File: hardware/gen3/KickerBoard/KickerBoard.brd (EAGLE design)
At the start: 130 x 100 mm, 104 parts, among them Q6 MOSFET-PCHANNEL, U1 NC7WZ08K8X, U2 ATMEGA165PV-8AU

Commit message: regulator
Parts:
- removed 5REG: (no value), SparkFun-PowerIC:SOT23-5
- removed C7: 470pF, SparkFun-Capacitors:0805
- added U$6: 3.3REG1A, gen3:3.3REG1A
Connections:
- removed net N$16: 5REG.4, C7.1
- net 12V: now also U$6.FIN, U$6.IN; no longer 5REG.1, 5REG.3
- net 5V: now also U$6.OUT; no longer 5REG.5
- net GND: now also U$6.NC; no longer 5REG.2, C7.2
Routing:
- net 12V: track 403.9 -> 394.5 mm
- net GND: track 496.7 -> 493.5 mm
- net N$16: track 3.19 -> 0.00 mm
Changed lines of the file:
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@@
 <attribute name="PROD_ID" value="VREG-00822" x="-55.12" y="144.31" size="1.778" layer="27" rot="R180" display="off"/>
-</element>
-<element name="5REG" library="SparkFun-PowerIC" package="SOT23-5" value="" x="16" y="21.5">
-<attribute name="PROD_ID" value="VREG-00823" x="90.93" y="-109.31" size="1.778" layer="27" display="off"/>
 </element>
 <element name="BATT" library="con-wago-500" package="W237-102" value="" x="38" y="7">
@@
 <element name="PWM_FILT" library="gen3" package="TESTING_PT" value="TEST_PT" x="58.2" y="66" rot="R180"/>
 <element name="DIS" library="gen3" package="TESTING_PT" value="TEST_PT" x="112" y="15"/>
-<element name="C7" library="SparkFun-Capacitors" package="0805" value="470pF" x="20" y="20.5"/>
 <element name="C8" library="SparkFun-Capacitors" package="0805" value="470pF" x="20" y="14.5"/>
 <element name="C10" library="gen3" package="PANASONIC_D" value="100uF" x="26" y="12.5" rot="R270">
@@
 </element>
 <element name="R9" library="SparkFun-Passives" package="0805" value="10k" x="21.3" y="71.2" rot="R270"/>
+<element name="U$6" library="gen3" package="3.3REG1A" value="3.3REG1A" x="-104" y="6"/>
 </elements>
 <signals>
@@
 <wire x1="70.262" y1="66.5776" x2="70.262" y2="66.238" width="0.3048" layer="1"/>
 <wire x1="64.05" y1="67.95" x2="63.2499" y2="67.95" width="0.4064" layer="1"/>
-<contactref element="C7" pad="2"/>
 <contactref element="C8" pad="2"/>
 <contactref element="C10" pad="-"/>
@@
 <contactref element="C21" pad="2"/>
 <contactref element="3.3REG" pad="2"/>
-<contactref element="5REG" pad="2"/>
 <wire x1="39.76" y1="14.18" x2="39.0230875" y2="14.248475" width="6.4516" layer="1"/>
 <wire x1="39.0230875" y1="14.248475" x2="39.3962" y2="17.0472125" width="6.4516" layer="1"/>
@@
 <wire x1="24" y1="17.5" x2="23.25" y2="18.25" width="1.6764" layer="1"/>
 <wire x1="23.25" y1="18.25" x2="21" y2="20.5" width="1.6764" layer="1"/>
-<wire x1="21" y1="20.5" x2="20.9" y2="20.5" width="1.6764" layer="1"/>
 <wire x1="24" y1="17.5" x2="21" y2="14.5" width="1.6764" layer="1"/>
 <wire x1="21" y1="14.5" x2="20.9" y2="14.5" width="1.6764" layer="1"/>
-<wire x1="20.9" y1="20.5" x2="21" y2="22.6" width="1.6764" layer="1"/>
 <wire x1="20.9" y1="14.5" x2="20.4" y2="11.6" width="1.6764" layer="1"/>
-<wire x1="16" y1="20.1999" x2="16" y2="19.2" width="0.4064" layer="1"/>
 <wire x1="16" y1="19.2" x2="16.8" y2="18.4" width="0.4064" layer="1"/>
 <wire x1="16.8" y1="17.6" x2="16.8" y2="16.9" width="0.4064" layer="1"/>
@@
 <vertex x="6" y="99"/>
 </polygon>
+<contactref element="U$6" pad="NC"/>
+<wire x1="3.3" y1="7.7" x2="-104" y2="2.69" width="0" layer="19" extent="1-1"/>
+<wire x1="21" y1="22.6" x2="21" y2="20.5" width="0" layer="19" extent="1-1"/>
 </signal>
 <signal name="3.3V">
@@
 <contactref element="DRIB" pad="1"/>
 <contactref element="3.3REG" pad="3"/>
-<contactref element="5REG" pad="1"/>
-<contactref element="5REG" pad="3"/>
 <contactref element="3.3REG" pad="1"/>
 <contactref element="U$3" pad="P$5"/>
@@
 <wire x1="82.5" y1="67" x2="82.5" y2="68" width="1.778" layer="1"/>
 <wire x1="63.63" y1="36.63" x2="59.88" y2="36.63" width="1.778" layer="1"/>
-<wire x1="15.05" y1="20.1999" x2="15.05" y2="14.8001" width="0.6096" layer="1"/>
-<wire x1="15.05" y1="20.1999" x2="15" y2="20.1499" width="0.6096" layer="1"/>
 <wire x1="15" y1="20.1499" x2="15" y2="17.5" width="0.6096" layer="1"/>
 <via x="15" y="17.5" extent="1-16" drill="0.6" shape="square"/>
@@
 <wire x1="17.301" y1="54.699" x2="12.5" y2="54.699" width="3.81" layer="1"/>
 <wire x1="15" y1="17.5" x2="14.95" y2="17.5" width="1.6764" layer="1"/>
-<wire x1="16.95" y1="20.1999" x2="16.95" y2="21.05" width="0.4064" layer="1"/>
-<wire x1="16.95" y1="21.05" x2="16.5" y2="21.5" width="0.4064" layer="1"/>
-<wire x1="16.5" y1="21.5" x2="15.5" y2="21.5" width="0.4064" layer="1"/>
-<wire x1="15.5" y1="21.5" x2="15.1" y2="21.1" width="0.4064" layer="1"/>
-<wire x1="15.1" y1="21.1" x2="15.1" y2="20.2499" width="0.4064" layer="1"/>
-<wire x1="15.1" y1="20.2499" x2="15.05" y2="20.1999" width="0.4064" layer="1"/>
 <wire x1="15.05" y1="14.8001" x2="15.05" y2="13.85" width="0.4064" layer="1"/>
 <wire x1="15.05" y1="13.85" x2="15.4" y2="13.8" width="0.4064" layer="1"/>
@@
 <vertex x="5.5" y="99"/>
 </polygon>
+<contactref element="U$6" pad="FIN"/>
+<contactref element="U$6" pad="IN"/>
+<wire x1="-104" y1="8.5" x2="-106.28" y2="1.2" width="0" layer="19" extent="1-1"/>
+<wire x1="15.05" y1="13.85" x2="-104" y2="8.5" width="0" layer="19" extent="1-1"/>
+<wire x1="16.95" y1="17.5" x2="16.95" y2="14.8001" width="0" layer="19" extent="1-16"/>
 </signal>
 <signal name="12VGND">
@@
 </signal>
 <signal name="5V">
-<contactref element="5REG" pad="5"/>
 <contactref element="LOGIC_HEADER" pad="5"/>
 <contactref element="LOGIC_HEADER" pad="6"/>
@@
 <wire x1="25.7" y1="25.5" x2="21" y2="25.5" width="1.6764" layer="1"/>
 <wire x1="21" y1="25.5" x2="21" y2="24.4" width="0.6096" layer="1"/>
-<wire x1="15.05" y1="22.8001" x2="15" y2="22.8501" width="0.6096" layer="1"/>
 <wire x1="15" y1="22.8501" x2="15" y2="25.5" width="0.6096" layer="1"/>
 <wire x1="15" y1="25.5" x2="21" y2="25.5" width="1.6764" layer="1"/>
@@
 <wire x1="66.95" y1="73.7" x2="66.960646875" y2="72.989353125" width="1.27" layer="1"/>
 <wire x1="66.960646875" y1="72.989353125" x2="66.960646875" y2="69.385609375" width="1.27" layer="1"/>
+<contactref element="U$6" pad="OUT"/>
+<wire x1="8" y1="14.16" x2="-101.72" y2="1.2" width="0" layer="19" extent="1-1"/>
 </signal>
 <signal name="N$19">
@@
 <wire x1="22.7" y1="82.5" x2="22.4" y2="82.6" width="0.254" layer="1"/>
 </signal>
-<signal name="N$16">
-<contactref element="5REG" pad="4"/>
-<contactref element="C7" pad="1"/>
-<wire x1="16.95" y1="22.8001" x2="16.95" y2="22.65" width="0.4064" layer="1"/>
-<wire x1="16.95" y1="22.65" x2="19.1" y2="20.5" width="0.4064" layer="1"/>
-</signal>
 <signal name="N$18">

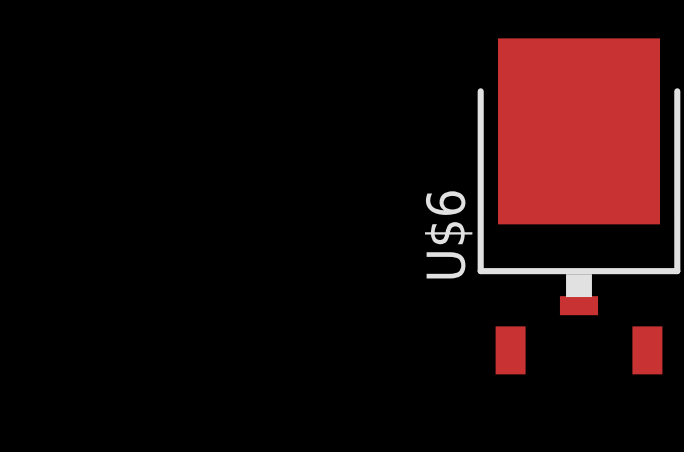
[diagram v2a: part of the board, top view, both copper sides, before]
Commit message: added decoupling to comms and kicker
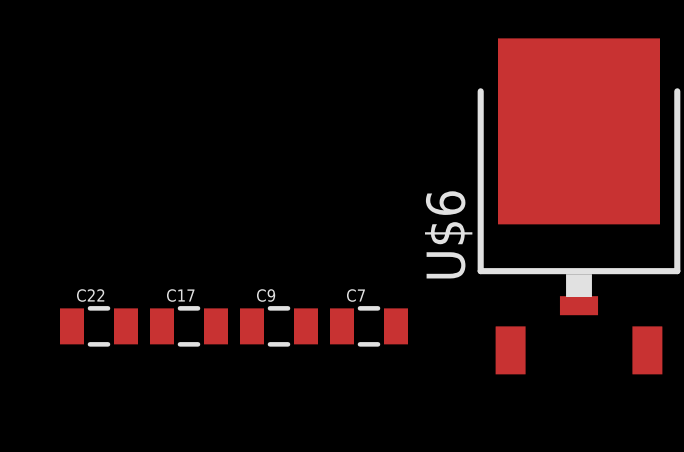
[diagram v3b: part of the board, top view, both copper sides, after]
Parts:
- added C17: 1uF, SparkFun-Capacitors:0805
- added C22, C7, C9: .01uF, SparkFun-Capacitors:0805
- C13, C14: value .1uF -> 1uF
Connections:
- net 3.3V: now also C17.1, C22.1, C7.1
- net 5V: now also C9.1
- net GND: now also C17.2, C22.2, C7.2, C9.2
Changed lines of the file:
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@@
 <element name="LED6" library="SparkFun-LED" package="LED-1206" value="" x="5" y="34" rot="R180"/>
 <element name="LED7" library="SparkFun-LED" package="LED-1206" value="" x="5" y="30" rot="R180"/>
-<element name="C13" library="SparkFun-Capacitors" package="0805" value=".1uF" x="20.4" y="10.7" rot="R90"/>
-<element name="C14" library="SparkFun-Capacitors" package="0805" value=".1uF" x="21" y="23.5" rot="R270"/>
+<element name="C13" library="SparkFun-Capacitors" package="0805" value="1uF" x="20.4" y="10.7" rot="R90"/>
+<element name="C14" library="SparkFun-Capacitors" package="0805" value="1uF" x="21" y="23.5" rot="R270"/>
 <element name="C15" library="SparkFun-Capacitors" package="0805" value=".1uF" x="54.65" y="65.75" rot="R270"/>
 <element name="C16" library="SparkFun-Capacitors" package="0805" value=".1uF" x="83" y="71"/>
@@
 <element name="R9" library="SparkFun-Passives" package="0805" value="10k" x="21.3" y="71.2" rot="R270"/>
 <element name="U$6" library="gen3" package="3.3REG1A" value="3.3REG1A" x="-104" y="6"/>
+<element name="C7" library="SparkFun-Capacitors" package="0805" value=".01uF" x="-111" y="2"/>
+<element name="C9" library="SparkFun-Capacitors" package="0805" value=".01uF" x="-114" y="2"/>
+<element name="C17" library="SparkFun-Capacitors" package="0805" value="1uF" x="-117" y="2"/>
+<element name="C22" library="SparkFun-Capacitors" package="0805" value=".01uF" x="-120" y="2"/>
 </elements>
 <signals>
@@
 </polygon>
 <contactref element="U$6" pad="NC"/>
+<contactref element="C7" pad="2"/>
+<contactref element="C9" pad="2"/>
+<contactref element="C22" pad="2"/>
+<contactref element="C17" pad="2"/>
+<wire x1="-116.1" y1="2" x2="-119.1" y2="2" width="0" layer="19" extent="1-1"/>
+<wire x1="-113.1" y1="2" x2="-116.1" y2="2" width="0" layer="19" extent="1-1"/>
+<wire x1="-110.1" y1="2" x2="-113.1" y2="2" width="0" layer="19" extent="1-1"/>
+<wire x1="-104" y1="2.69" x2="-110.1" y2="2" width="0" layer="19" extent="1-1"/>
 <wire x1="3.3" y1="7.7" x2="-104" y2="2.69" width="0" layer="19" extent="1-1"/>
 <wire x1="21" y1="22.6" x2="21" y2="20.5" width="0" layer="19" extent="1-1"/>
@@
 <wire x1="79.7" y1="53.7" x2="79.7" y2="58.95" width="0.8128" layer="1"/>
 <wire x1="79.7" y1="58.95" x2="79.8" y2="59.05" width="0.8128" layer="1"/>
+<contactref element="C7" pad="1"/>
+<contactref element="C17" pad="1"/>
+<contactref element="C22" pad="1"/>
+<wire x1="-117.9" y1="2" x2="-120.9" y2="2" width="0" layer="19" extent="1-1"/>
+<wire x1="-111.9" y1="2" x2="-117.9" y2="2" width="0" layer="19" extent="1-1"/>
+<wire x1="7.5" y1="11.5" x2="-111.9" y2="2" width="0" layer="19" extent="1-1"/>
 </signal>
 <signal name="MOSI">
@@
 <wire x1="66.960646875" y1="72.989353125" x2="66.960646875" y2="69.385609375" width="1.27" layer="1"/>
 <contactref element="U$6" pad="OUT"/>
+<contactref element="C9" pad="1"/>
+<wire x1="-101.72" y1="1.2" x2="-114.9" y2="2" width="0" layer="19" extent="1-1"/>
 <wire x1="8" y1="14.16" x2="-101.72" y2="1.2" width="0" layer="19" extent="1-1"/>
 </signal>

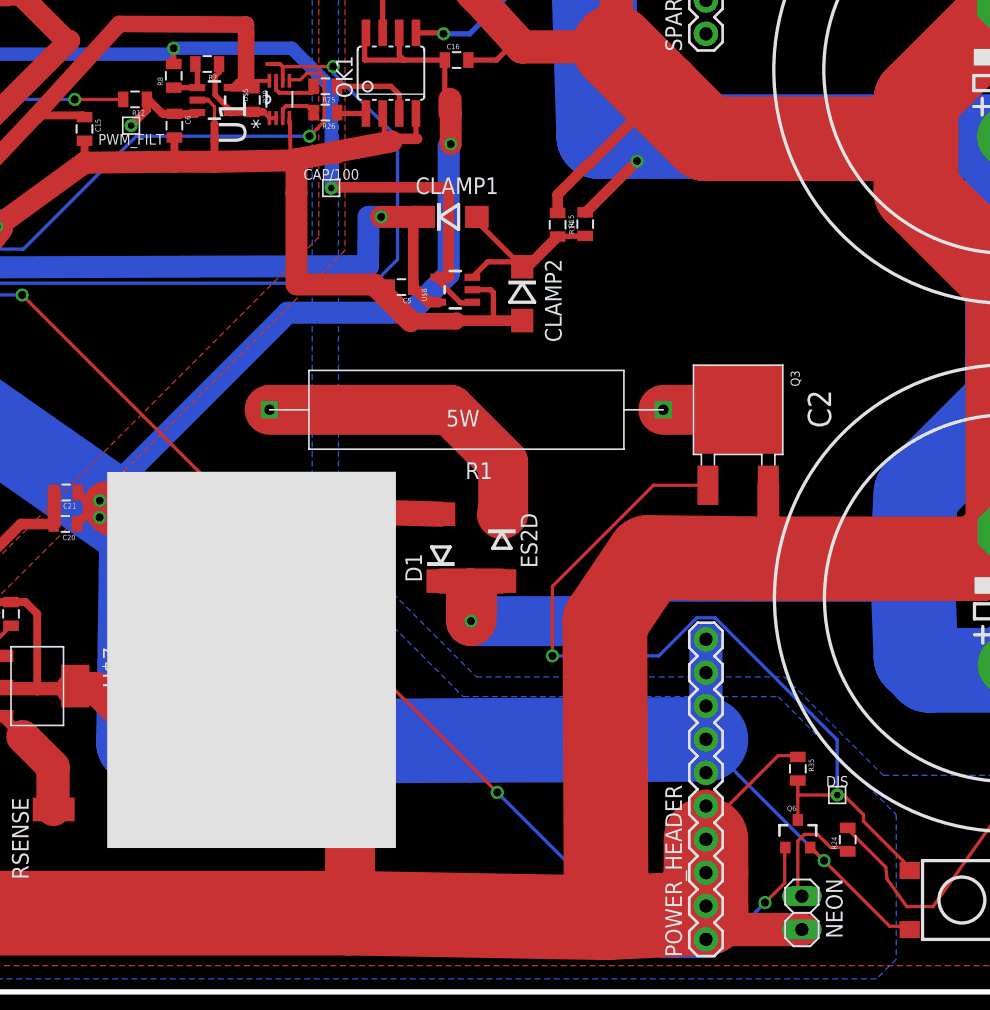
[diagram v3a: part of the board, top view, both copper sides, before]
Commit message: fixed voltage values on kicker
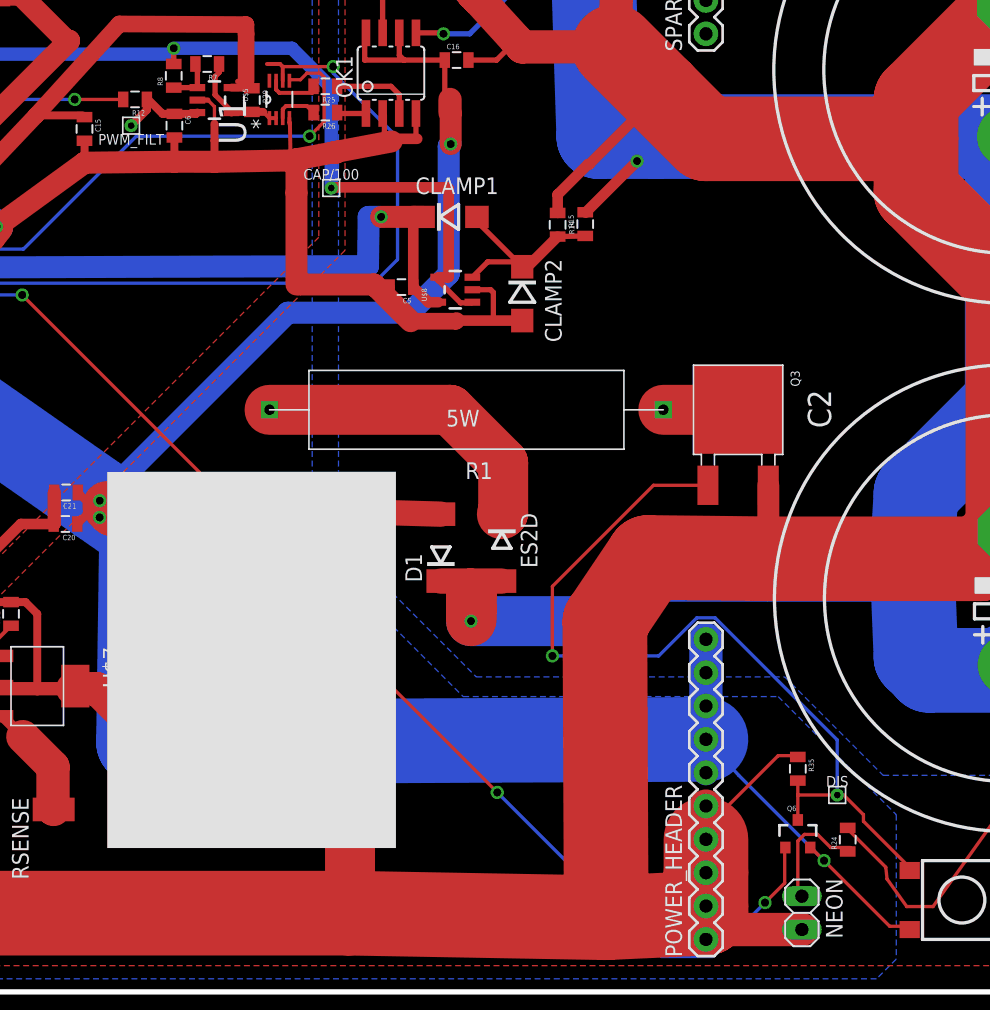
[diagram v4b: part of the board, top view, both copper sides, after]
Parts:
- R25, R26: value 200 -> 100
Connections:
- net 12V: no longer MAN-DIS.B2, Q6.2
- net 3.3V: now also C15.1, MAN-DIS.B2, Q6.2, R29.1, U$5.5, U1.8
- net 5V: no longer C15.1, R29.1, U$5.5, U1.8
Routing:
- net 5V: track 128.7 -> 124.4 mm
- net 3.3V: track 249.4 -> 251.1 mm
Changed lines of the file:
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@@
 <element name="NEON" library="pinhead" package="1X02" value="" x="109.31" y="6.02" rot="R270"/>
 <element name="R24" library="SparkFun-Passives" package="0805" value="536k" x="112.8" y="11.6" rot="R90"/>
-<element name="R25" library="SparkFun-Passives" package="0805" value="200" x="73" y="69" rot="R180"/>
-<element name="R26" library="SparkFun-Passives" package="0805" value="200" x="73" y="67" rot="R180"/>
+<element name="R25" library="SparkFun-Passives" package="0805" value="100" x="73" y="69" rot="R180"/>
+<element name="R26" library="SparkFun-Passives" package="0805" value="100" x="73" y="67" rot="R180"/>
 <element name="R27" library="SparkFun-Passives" package="0805" value="1k" x="93" y="78" rot="R90"/>
 <element name="R28" library="SparkFun-Passives" package="0805" value="1k" x="80" y="78" rot="R90"/>
@@
 <contactref element="C17" pad="1"/>
 <contactref element="C22" pad="1"/>
-<wire x1="-117.9" y1="2" x2="-120.9" y2="2" width="0" layer="19" extent="1-1"/>
-<wire x1="-111.9" y1="2" x2="-117.9" y2="2" width="0" layer="19" extent="1-1"/>
-<wire x1="7.5" y1="11.5" x2="-111.9" y2="2" width="0" layer="19" extent="1-1"/>
+<contactref element="MAN-DIS" pad="B2"/>
+<contactref element="Q6" pad="2"/>
+<contactref element="R29" pad="1"/>
+<contactref element="U1" pad="8"/>
+<contactref element="C15" pad="1"/>
+<contactref element="U$5" pad="5"/>
+<wire x1="65.75" y1="68.95" x2="65.8501" y2="68.9" width="0.254" layer="1"/>
+<wire x1="67.4" y1="68.85" x2="67.35" y2="68.9" width="0.6096" layer="1"/>
+<wire x1="67.35" y1="68.9" x2="65.8501" y2="68.9" width="0.6096" layer="1"/>
+<wire x1="67.4" y1="68.85" x2="68.738" y2="69.4224" width="0" layer="19" extent="1-1"/>
+<wire x1="54.65" y1="66.65" x2="65.75" y2="68.95" width="0" layer="19" extent="1-1"/>
+<wire x1="53.475" y1="72.475" x2="54.65" y2="66.65" width="0" layer="19" extent="1-1"/>
+<wire x1="109.95" y1="11" x2="81.5999" y2="52.55" width="0" layer="19" extent="1-1"/>
+<wire x1="117.525" y1="4.75" x2="109.95" y2="11" width="0" layer="19" extent="1-1"/>
+<wire x1="-111.9" y1="2" x2="7.5" y2="11.5" width="0" layer="19" extent="1-1"/>
+<wire x1="-117.9" y1="2" x2="-111.9" y2="2" width="0" layer="19" extent="1-1"/>
+<wire x1="-120.9" y1="2" x2="-117.9" y2="2" width="0" layer="19" extent="1-1"/>
 </signal>
 <signal name="MOSI">
@@
 <wire x1="82.1" y1="71" x2="82.1" y2="68.4" width="0.4064" layer="1"/>
 <wire x1="82.1" y1="68.4" x2="82.5" y2="68" width="0.4064" layer="1"/>
-<contactref element="MAN-DIS" pad="B2"/>
-<contactref element="Q6" pad="2"/>
 <contactref element="R10" pad="2"/>
 <contactref element="12V" pad="P$1"/>
@@
 <wire x1="111" y1="10" x2="110" y2="11" width="0.254" layer="1"/>
 <wire x1="117.5" y1="5" x2="116" y2="5" width="0.254" layer="1"/>
-<wire x1="110" y1="11" x2="109.95" y2="11" width="0.254" layer="1"/>
-<wire x1="117.5" y1="5" x2="117.525" y2="4.75" width="0.254" layer="1"/>
 <wire x1="34" y1="49" x2="36.90746875" y2="53.865946875" width="0.254" layer="16"/>
 <wire x1="104.5" y1="16.5" x2="111" y2="10" width="0.254" layer="16"/>
@@
 <contactref element="LOGIC_HEADER" pad="5"/>
 <contactref element="LOGIC_HEADER" pad="6"/>
-<contactref element="R29" pad="1"/>
-<contactref element="U1" pad="8"/>
 <contactref element="C14" pad="1"/>
-<contactref element="C15" pad="1"/>
-<contactref element="U$5" pad="5"/>
-<wire x1="68.738" y1="69.4224" x2="66.960646875" y2="69.385609375" width="0.3048" layer="1"/>
 <wire x1="66.960646875" y1="69.385609375" x2="66.3225" y2="69.3724" width="0.4064" layer="1"/>
-<wire x1="66.3225" y1="69.3724" x2="65.8501" y2="68.9" width="0.4064" layer="1"/>
 <contactref element="5V" pad="P$1"/>
 <contactref element="C11" pad="+"/>
@@
 <wire x1="25.8" y1="25.4" x2="26" y2="25.2" width="2.54" layer="1"/>
 <wire x1="12" y1="20" x2="11.659221875" y2="19.995246875" width="0.254" layer="1"/>
-<wire x1="65.75" y1="68.95" x2="65.8501" y2="68.9" width="0.254" layer="1"/>
 <wire x1="27" y1="25.5" x2="25.8" y2="25.4" width="0.254" layer="1"/>
 <wire x1="27" y1="25.5" x2="26" y2="26.5" width="1.27" layer="1"/>
@@
 <wire x1="29.65" y1="44.3" x2="50.9611375" y2="66.784228125" width="1.27" layer="1"/>
 <wire x1="50.9611375" y1="66.784228125" x2="57.3" y2="73.75" width="1.27" layer="1"/>
-<wire x1="67.4" y1="68.85" x2="67.35" y2="68.9" width="0.6096" layer="1"/>
-<wire x1="67.35" y1="68.9" x2="65.8501" y2="68.9" width="0.6096" layer="1"/>
-<wire x1="54.65" y1="66.65" x2="54.515771875" y2="66.784228125" width="0.6096" layer="1"/>
 <wire x1="54.515771875" y1="66.784228125" x2="50.9611375" y2="66.784228125" width="0.6096" layer="1"/>
 <wire x1="57.3" y1="73.75" x2="66.95" y2="73.7" width="1.27" layer="1"/>
